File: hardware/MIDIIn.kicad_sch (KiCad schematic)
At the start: 6 parts, among them J301 SJ2-25404B-SMT-TR, U301 TLP2361

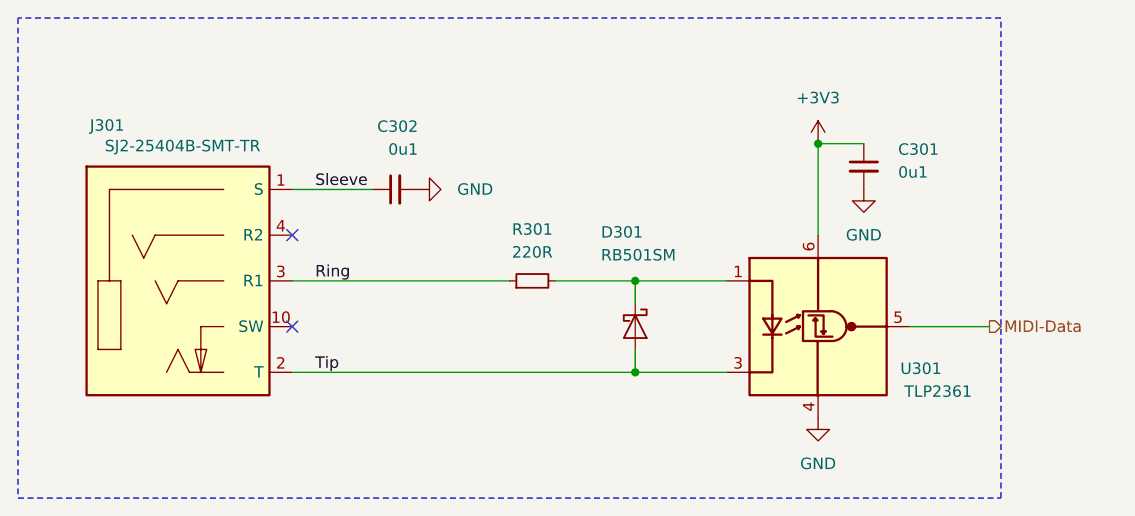
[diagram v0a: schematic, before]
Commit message: Update symbols
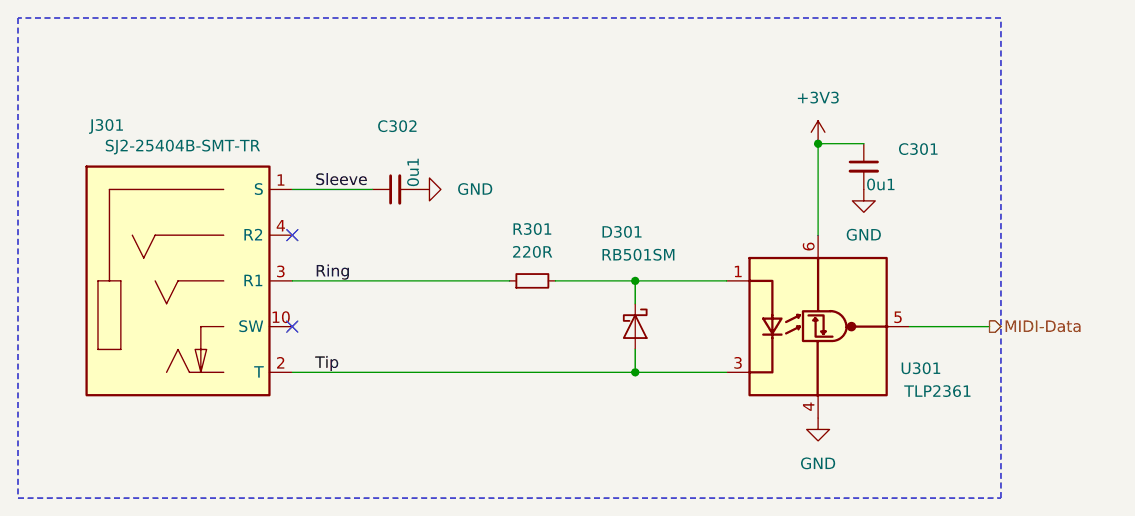
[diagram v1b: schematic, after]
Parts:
- C301, C302: footprint Capacitor_SMD:C_0603_1608Metric -> V2_Capacitor_SMD:C_0603; symbol Device:C_Small -> V2_Device:C_0603_0u1; Mouser (none) -> 810-CGA3E2X7R1H104MA
- D301: footprint Diode_SMD:D_SOD-523 -> V2_Diode_SMD:D_SOD-523; Mouser (none) -> 755-RB501SM-30FHT2R
- J301: Mouser (none) -> 490-SJ2-25404BSMT-TR
- R301: footprint Resistor_SMD:R_0603_1608Metric -> V2_Resistor_SMD:R_0603; symbol Device:R_Small -> V2_Device:R_0603_220R; Mouser (none) -> 71-CRCW0603220RFKEAH
- U301: footprint Package_SO:SO-5-6_4.55x3.7mm_P1.27mm -> V2_Package_SO:SO-5-6_4.55x3.7mm_P1.27mm; Mouser (none) -> 757-TLP2361TPRE
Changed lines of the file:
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@@
 			)
 		)
-		(property "Description" "SJ2-35464B-SMT-TR"
+		(property "Description" ""
 			(at 108.712 131.064 0)
 			(effects
@@
 				)
 				(justify left bottom)
+				(hide yes)
+			)
+		)
+		(property "Mouser" " 490-SJ2-25404BSMT-TR"
+			(at 116.84 107.95 0)
+			(effects
+				(font
+					(size 1.27 1.27)
+				)
 				(hide yes)
 			)
@@
 	)
 	(symbol
-		(lib_id "Device:C_Small")
+		(lib_id "V2_Device:C_0603_0u1")
 		(at 140.97 97.79 90)
 		(unit 1)
@@
 		)
 		(property "Value" "0u1"
-			(at 143.5162 93.345 90)
-			(effects
-				(font
-					(size 1.27 1.27)
-				)
-				(justify left)
-			)
-		)
-		(property "Footprint" "Capacitor_SMD:C_0603_1608Metric"
+			(at 143.002 97.536 0)
+			(effects
+				(font
+					(size 1.27 1.27)
+				)
+				(justify left)
+			)
+		)
+		(property "Footprint" "V2_Capacitor_SMD:C_0603"
+			(at 157.988 97.79 0)
+			(effects
+				(font
+					(size 1.27 1.27)
+				)
+				(hide yes)
+			)
+		)
+		(property "Datasheet" ""
 			(at 140.97 97.79 0)
 			(effects
@@
 			)
 		)
-		(property "Datasheet" "~"
-			(at 140.97 97.79 0)
-			(effects
-				(font
-					(size 1.27 1.27)
-				)
-				(hide yes)
-			)
-		)
 		(property "Description" "Unpolarized capacitor, small symbol"
-			(at 140.97 97.79 0)
+			(at 154.432 97.79 0)
+			(effects
+				(font
+					(size 1.27 1.27)
+				)
+				(hide yes)
+			)
+		)
+		(property "Mouser" " 810-CGA3E2X7R1H104MA"
+			(at 161.29 97.79 0)
 			(effects
 				(font
@@
 			)
 		)
-		(property "Footprint" "Package_SO:SO-5-6_4.55x3.7mm_P1.27mm"
+		(property "Footprint" "V2_Package_SO:SO-5-6_4.55x3.7mm_P1.27mm"
 			(at 170.18 125.73 0)
 			(effects
@@
 		)
 		(property "Datasheet" ""
-			(at 185.2168 112.395 0)
+			(at 150.9268 144.145 0)
 			(effects
 				(font
@@
 			)
 		)
+		(property "Mouser" " 757-TLP2361TPRE"
+			(at 187.96 113.03 0)
+			(effects
+				(font
+					(size 1.27 1.27)
+				)
+				(hide yes)
+			)
+		)
 		(pin "1"
 		)
@@
 	)
 	(symbol
-		(lib_id "Device:C_Small")
+		(lib_id "V2_Device:C_0603_0u1")
 		(at 193.04 95.25 0)
 		(unit 1)
@@
 		)
 		(property "Value" "0u1"
-			(at 196.85 95.8912 0)
-			(effects
-				(font
-					(size 1.27 1.27)
-				)
-				(justify left)
-			)
-		)
-		(property "Footprint" "Capacitor_SMD:C_0603_1608Metric"
+			(at 193.294 97.282 0)
+			(effects
+				(font
+					(size 1.27 1.27)
+				)
+				(justify left)
+			)
+		)
+		(property "Footprint" "V2_Capacitor_SMD:C_0603"
+			(at 193.04 112.268 0)
+			(effects
+				(font
+					(size 1.27 1.27)
+				)
+				(hide yes)
+			)
+		)
+		(property "Datasheet" ""
 			(at 193.04 95.25 0)
 			(effects
@@
 			)
 		)
-		(property "Datasheet" "~"
-			(at 193.04 95.25 0)
-			(effects
-				(font
-					(size 1.27 1.27)
-				)
-				(hide yes)
-			)
-		)
 		(property "Description" "Unpolarized capacitor, small symbol"
-			(at 193.04 95.25 0)
+			(at 193.04 108.712 0)
+			(effects
+				(font
+					(size 1.27 1.27)
+				)
+				(hide yes)
+			)
+		)
+		(property "Mouser" " 810-CGA3E2X7R1H104MA"
+			(at 193.04 115.57 0)
 			(effects
 				(font
@@
 			)
 		)
-		(property "Footprint" "Diode_SMD:D_SOD-523"
+		(property "Footprint" "V2_Diode_SMD:D_SOD-523"
 			(at 160.655 113.03 0)
 			(effects
@@
 			)
 		)
+		(property "Mouser" " 755-RB501SM-30FHT2R"
+			(at 156.972 113.03 0)
+			(effects
+				(font
+					(size 1.27 1.27)
+				)
+				(hide yes)
+			)
+		)
 		(pin "1"
 		)
@@
 	)
 	(symbol
-		(lib_id "Device:R_Small")
+		(lib_id "V2_Device:R_0603_220R")
 		(at 156.21 107.95 90)
 		(unit 1)
@@
 			)
 		)
-		(property "Footprint" "Resistor_SMD:R_0603_1608Metric"
+		(property "Footprint" "V2_Resistor_SMD:R_0603"
+			(at 171.958 107.95 0)
+			(effects
+				(font
+					(size 1.27 1.27)
+				)
+				(hide yes)
+			)
+		)
+		(property "Datasheet" ""
 			(at 156.21 107.95 0)
 			(effects
@@
 			)
 		)
-		(property "Datasheet" "~"
-			(at 156.21 107.95 0)
-			(effects
-				(font
-					(size 1.27 1.27)
-				)
-				(hide yes)
-			)
-		)
 		(property "Description" "Resistor, small symbol"
-			(at 156.21 107.95 0)
-			(effects
-				(font
+			(at 168.402 107.95 0)
+			(effects
+				(font
+					(size 1.27 1.27)
+				)
+				(hide yes)
+			)
+		)
+		(property "Mouser" " 71-CRCW0603220RFKEAH"
+			(at 175.26 107.95 0)
+			(effects
+				(font

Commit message: Refresh
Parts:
- C301, C302: Mouser 810-CGA3E2X7R1H104MA -> 810-CGA3E2X7R1H104MA
- R301: Mouser 71-CRCW0603220RFKEAH -> 71-CRCW0603220RFKEAH
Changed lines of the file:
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@@
 			)
 		)
-		(property "Mouser" " 810-CGA3E2X7R1H104MA"
+		(property "Mouser" "810-CGA3E2X7R1H104MA"
 			(at 161.29 97.79 0)
 			(effects
@@
 			)
 		)
-		(property "Mouser" " 810-CGA3E2X7R1H104MA"
+		(property "Mouser" "810-CGA3E2X7R1H104MA"
 			(at 193.04 115.57 0)
 			(effects
@@
 			)
 		)
-		(property "Mouser" " 71-CRCW0603220RFKEAH"
+		(property "Mouser" "71-CRCW0603220RFKEAH"
 			(at 175.26 107.95 0)
 			(effects

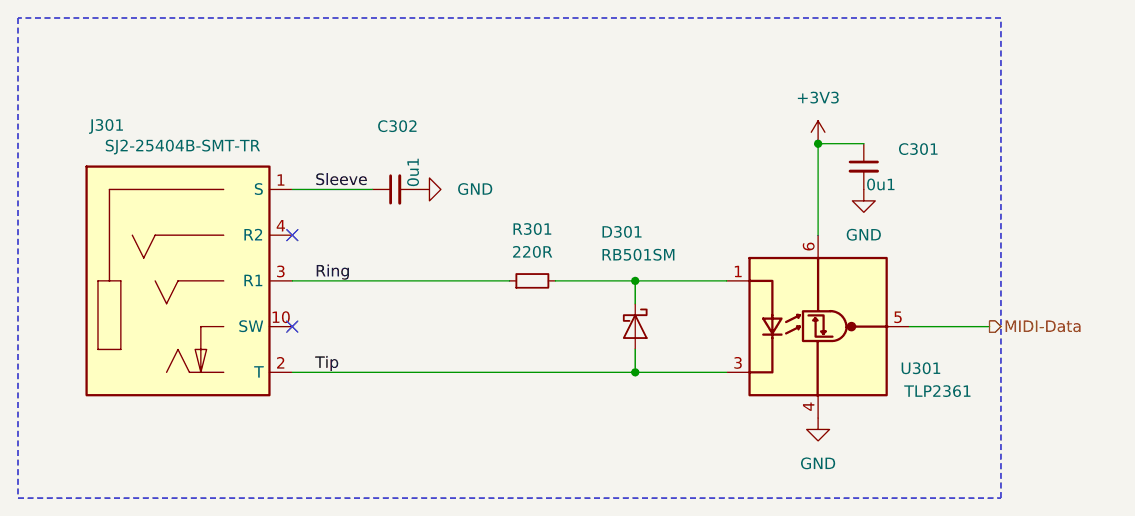
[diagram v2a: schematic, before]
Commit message: Update power symbols
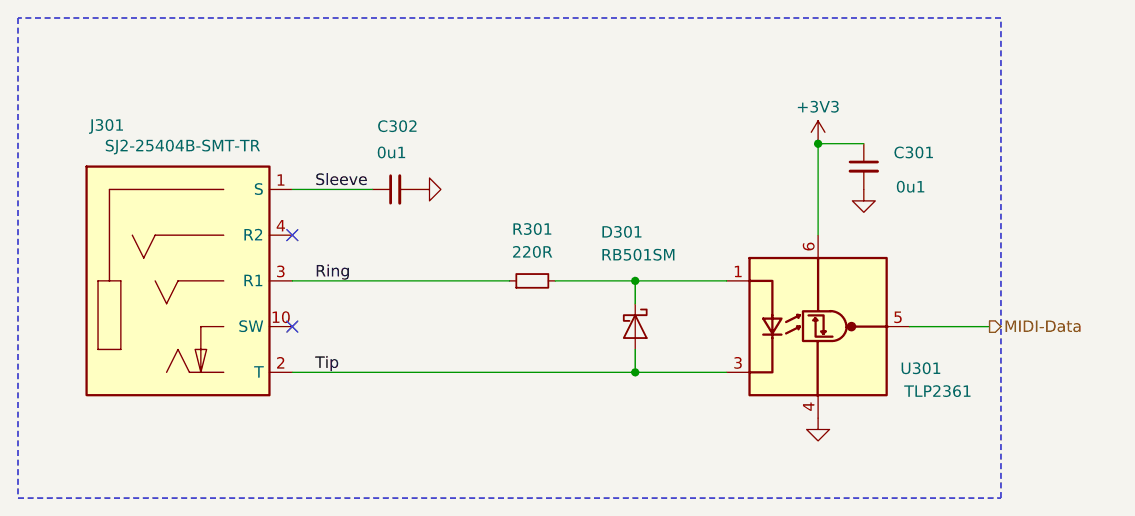
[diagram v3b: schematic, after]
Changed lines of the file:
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@@
 	)
 	(symbol
-		(lib_id "power:GND")
+		(lib_id "V2_power:GND")
 		(at 143.51 97.79 90)
 		(unit 1)
@@
 		)
 		(property "Value" "GND"
-			(at 149.86 97.79 90)
-			(effects
-				(font
-					(size 1.27 1.27)
-				)
+			(at 147.574 97.79 0)
+			(effects
+				(font
+					(size 1.27 1.27)
+				)
+				(hide yes)
 			)
 		)
@@
 		)
 		(property "Description" "Power symbol creates a global label with name \"GND\" , ground"
-			(at 143.51 97.79 0)
+			(at 153.924 98.044 0)
 			(effects
 				(font
@@
 		)
 		(property "Value" "0u1"
-			(at 143.002 97.536 0)
+			(at 142.24 93.726 90)
 			(effects
 				(font
@@
 		(dnp no)
 		(property "Reference" "C301"
-			(at 196.85 93.3512 0)
+			(at 196.342 93.726 0)
 			(effects
 				(font
@@
 		)
 		(property "Value" "0u1"
-			(at 193.294 97.282 0)
+			(at 196.596 97.536 0)
 			(effects
 				(font
@@
 	)
 	(symbol
-		(lib_id "power:GND")
+		(lib_id "V2_power:GND")
 		(at 187.96 123.19 0)
 		(unit 1)
@@
 		)
 		(property "Value" "GND"
-			(at 187.96 128.27 0)
-			(effects
-				(font
-					(size 1.27 1.27)
-				)
+			(at 187.96 127.254 0)
+			(effects
+				(font
+					(size 1.27 1.27)
+				)
+				(hide yes)
 			)
 		)
@@
 		)
 		(property "Description" "Power symbol creates a global label with name \"GND\" , ground"
-			(at 187.96 123.19 0)
+			(at 187.706 133.604 0)
 			(effects
 				(font
@@
 	)
 	(symbol
-		(lib_id "power:+3V3")
+		(lib_id "V2_power:+3V3")
 		(at 187.96 92.71 0)
 		(unit 1)
@@
 		)
 		(property "Value" "+3V3"
-			(at 187.96 87.63 0)
+			(at 187.96 88.646 0)
 			(effects
 				(font
@@
 		)
 		(property "Description" "Power symbol creates a global label with name \"+3V3\""
-			(at 187.96 92.71 0)
+			(at 187.96 107.696 0)
 			(effects
 				(font
@@
 	)
 	(symbol
-		(lib_id "power:GND")
+		(lib_id "V2_power:GND")
 		(at 193.04 97.79 0)
 		(unit 1)
@@
 		)
 		(property "Value" "GND"
-			(at 193.04 102.87 0)
-			(effects
-				(font
-					(size 1.27 1.27)
-				)
+			(at 193.04 101.854 0)
+			(effects
+				(font
+					(size 1.27 1.27)
+				)
+				(hide yes)
 			)
 		)
@@
 		)
 		(property "Description" "Power symbol creates a global label with name \"GND\" , ground"
-			(at 193.04 97.79 0)
-			(effects
-				(font
+			(at 192.786 108.204 0)
+			(effects
+				(font

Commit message: Update parts
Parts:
- C301, C302: Manufacturer (none) -> TDK; Product (none) -> CGA3E2X7R1H104M080AA
- D301: Manufacturer (none) -> ROHM Semiconductor; Mouser 755-RB501SM-30FHT2R -> 755-RB501SM-30FHT2R; Product (none) -> RB501SM-30FHT2R
- J301: Manufacturer (none) -> Same Sky; Mouser 490-SJ2-25404BSMT-TR -> 490-SJ2-25404BSMT-TR; Product (none) -> SJ2-25404B-SMT-TR
- R301: Manufacturer (none) -> Vishay; Product (none) -> CRCW0603220RFKEAHP; Rating (none) -> 330mW
- U301: Manufacturer (none) -> Toshiba; Mouser 757-TLP2361TPRE -> 757-TLP2361TPRE; Product (none) -> TLP2361(TPR,E

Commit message: Refresh
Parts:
- C301, C302: Rating (none) -> 50V

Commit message: Update Library
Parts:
- C301, C302: symbol V2_Device:C_0603_0u1 -> V2_Capacitor:0603_0u1
- R301: symbol V2_Device:R_0603_220R -> V2_Resistor:0603_220R
